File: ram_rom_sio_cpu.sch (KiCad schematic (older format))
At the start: 13 parts, among them U1 SST39SF040, U2 Z84C0010AEG, U3 AS6C4008A-55ZIN, U4 Z84C4310AEG

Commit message: rotated layout
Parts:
- removed JP2: WR Ena, Connector_PinHeader_2.54mm:PinHeader_1x03_P2.54mm_Vertical, symbol Jumper:Jumper_3_Bridged12
- added J4: Port A, Connector_PinHeader_2.54mm:PinHeader_1x06_P2.54mm_Vertical, symbol Connector_Generic:Conn_01x06
- added R10, R7, R8, R9: 10K, Resistor_SMD:R_0603_1608Metric_Pad1.05x0.95mm_HandSolder, symbol Device:R_Small
- added R4, R6: 100K, Resistor_SMD:R_0603_1608Metric_Pad1.05x0.95mm_HandSolder, symbol Device:R_Small
- RN2: value 10K -> 2K2
- renumbered C3 to C2, C4 to C3, C5 to C4, C6 to C5, R9 to R2, R10 to R3, R11 to R5
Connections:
- net labels added: RX, TX, ~CTS, ~RTS
- net labels removed: RXA, ~CTSA, ~RTSA
- wire segments 157 -> 180
- no-connect marks 15 -> 16

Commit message: Routing completed, fixed RAM/ROM paging
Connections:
- net labels added: A[0..15], MA14, MA15, MA16, MA17, MA18, MA[14..18]
- net labels removed: A16, A17, A18, A[0..18], TXA
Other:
- moved on the sheet: R2

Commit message: added gnd plane stitching
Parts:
- U1: footprint Package_LCC:PLCC-32_11.4x14.0mm_P1.27mm -> Package_LCC:PLCC-32_11.4x14.0mm_P1.27mm-Socket
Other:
- note added: "SRAM 512K"
- moved on the sheet: C2, C3, C4, C5, J4, R2, R3, R4, R5, R6, RN2, U3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

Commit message: enhanced graphic for PLCC socket
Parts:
- removed U1: SST39SF040, Package_LCC:PLCC-32_11.4x14.0mm_P1.27mm-Socket, symbol Memory_Flash:SST39SF040
- added U?: SST39LF040, Package_LCC:PLCC-32_11.4x14.0mm_P1.27mm-Socket, symbol Memory_Flash:SST39LF040
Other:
- moved on the sheet: R2
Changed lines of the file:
@@
 L Device:R_Small R2
 U 1 1 5D959555
-P 10300 2000
-F 0 "R2" H 10359 2046 50  0000 L CNN
-F 1 "10K" H 10359 1955 50  0000 L CNN
-F 2 "Resistor_SMD:R_0603_1608Metric_Pad1.05x0.95mm_HandSolder" H 10300 2000 50  0001 C CNN
-F 3 "~" H 10300 2000 50  0001 C CNN
-	1    10300 2000
-	-1   0    0    -1
+P 7100 3200
+F 0 "R2" H 7159 3246 50  0000 L CNN
+F 1 "10K" H 7159 3155 50  0000 L CNN
+F 2 "Resistor_SMD:R_0603_1608Metric_Pad1.05x0.95mm_HandSolder" H 7100 3200 50  0001 C CNN
+F 3 "~" H 7100 3200 50  0001 C CNN
+	1    7100 3200
+	1    0    0    -1
 $EndComp
 $Comp
@@
 Text HLabel 9950 1500 2    50   3State ~ 0
 D[0..7]
-Text Label 9500 2100 0    50   ~ 0
+Text Label 7900 3300 2    50   ~ 0
 ROM_~CE
-Text HLabel 9700 2200 2    50   Input ~ 0
+Text HLabel 7700 3400 0    50   Input ~ 0
 ~RD
 Entry Wire Line
@@
 Wire Wire Line
 	9300 1100 9850 1100
-Text HLabel 10400 2100 2    50   Input ~ 0
+Text HLabel 7000 3300 0    50   Input ~ 0
 ROM_~CE~
 Text Notes 8950 900  0    50   ~ 0
 Flash/ROM
-$Comp
-L Memory_Flash:SST39SF040 U1
-U 1 1 5D653323
-P 8700 1950
-F 0 "U1" H 8350 3000 50  0000 C CNN
-F 1 "SST39SF040" H 8750 2000 50  0000 C CNN
-F 2 "Package_LCC:PLCC-32_11.4x14.0mm_P1.27mm-Socket" H 8700 2250 50  0001 C CNN
-F 3 "http://ww1.microchip.com/downloads/en/DeviceDoc/25022B.pdf" H 8700 2250 50  0001 C CNN
-	1    8700 1950
-	1    0    0    -1
-$EndComp
-Wire Wire Line
-	9300 2200 9700 2200
+Wire Wire Line
+	8100 3400 7700 3400
 Wire Wire Line
 	10200 5250 10300 5250
@@
 F 3 "" H 2900 750 50  0001 C CNN
 	1    2900 750
-	1    0    0    -1
-$EndComp
-$Comp
-L power:VCC #PWR?
-U 1 1 5DCF306D
-P 8700 1000
-AR Path="/5DCF306D" Ref="#PWR?"  Part="1"
-AR Path="/5D6224DC/5DCF306D" Ref="#PWR?"  Part="1"
-AR Path="/5F2A9FE8/5DCF306D" Ref="#PWR010"  Part="1"
-F 0 "#PWR010" H 8700 850 50  0001 C CNN
-F 1 "VCC" H 8717 1173 50  0000 C CNN
-F 2 "" H 8700 1000 50  0001 C CNN
-F 3 "" H 8700 1000 50  0001 C CNN
-	1    8700 1000
 	1    0    0    -1
 $EndComp
@@
 Text Label 3850 5550 0    50   ~ 0
 ~CTS
-Text HLabel 9700 2300 2    50   Input ~ 0
+Text HLabel 7700 3100 0    50   Input ~ 0
 ~WR
 Wire Wire Line
-	9300 2300 9700 2300
+	8100 3100 7700 3100
 $Comp
 L Device:R_Small R?
@@
 Text HLabel 7550 5950 0    50   Input ~ 0
 MA[14..18]
-$Comp
-L power:GND #PWR?
-U 1 1 5EB5C154
-P 8700 3050
-AR Path="/5EB5C154" Ref="#PWR?"  Part="1"
-AR Path="/5CB63856/5EB5C154" Ref="#PWR?"  Part="1"
-AR Path="/5CB5AB00/5CB63856/5EB5C154" Ref="#PWR?"  Part="1"
-AR Path="/5CFABACD/5EB5C154" Ref="#PWR?"  Part="1"
-AR Path="/5CF9C1ED/5EB5C154" Ref="#PWR?"  Part="1"
-AR Path="/5D6224DC/5EB5C154" Ref="#PWR?"  Part="1"
-AR Path="/5F2A9FE8/5EB5C154" Ref="#PWR0102"  Part="1"
-F 0 "#PWR0102" H 8700 2800 50  0001 C CNN
-F 1 "GND" H 8705 2877 50  0000 C CNN
-F 2 "" H 8700 3050 50  0001 C CNN
-F 3 "" H 8700 3050 50  0001 C CNN
-	1    8700 3050
-	1    0    0    -1
-$EndComp
-Wire Wire Line
-	9300 2100 10300 2100
-Wire Wire Line
-	10400 2100 10300 2100
-Connection ~ 10300 2100
+Wire Wire Line
+	8100 3300 7100 3300
+Wire Wire Line
+	7000 3300 7100 3300
+Connection ~ 7100 3300
 Text HLabel 7450 2800 0    50   Input ~ 0
 MA[14..18]
@@
 Text Notes 9050 3950 0    50   ~ 0
 SRAM 512K
+$Comp
+L Memory_Flash:SST39LF040 U?
+U 1 1 5EA5881D
+P 8700 2300
+F 0 "U?" H 8700 3781 50  0000 C CNN
+F 1 "SST39LF040" H 8700 3690 50  0000 C CNN
+F 2 "Package_LCC:PLCC-32_11.4x14.0mm_P1.27mm-Socket" H 8700 2600 50  0001 C CNN
+F 3 "http://ww1.microchip.com/downloads/en/DeviceDoc/25022B.pdf" H 8700 2600 50  0001 C CNN
+	1    8700 2300
+	1    0    0    -1
+$EndComp
 Wire Bus Line
 	1550 5700 1550 5850

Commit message: removed ram/rom ce pullups
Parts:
- removed R2, R3: 10K, Resistor_SMD:R_0603_1608Metric_Pad1.05x0.95mm_HandSolder, symbol Device:R_Small
- gave numbers to parts that had none: 1
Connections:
- net labels removed: RAM_~CE, ROM_~CE
- wire segments 180 -> 178
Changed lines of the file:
@@
 Wire Wire Line
 	9200 5350 9750 5350
-Text HLabel 10300 5250 2    50   Input ~ 0
+Text HLabel 9750 5250 2    50   Input ~ 0
 RAM_~CE~
 Text HLabel 9750 5350 2    50   Input ~ 0
@@
 	1    0    0    -1
 $EndComp
-$Comp
-L Device:R_Small R2
-U 1 1 5D959555
-P 7100 3200
-F 0 "R2" H 7159 3246 50  0000 L CNN
-F 1 "10K" H 7159 3155 50  0000 L CNN
-F 2 "Resistor_SMD:R_0603_1608Metric_Pad1.05x0.95mm_HandSolder" H 7100 3200 50  0001 C CNN
-F 3 "~" H 7100 3200 50  0001 C CNN
-	1    7100 3200
-	1    0    0    -1
-$EndComp
-$Comp
-L Device:R_Small R3
-U 1 1 5D966170
-P 10200 5150
-F 0 "R3" H 10259 5196 50  0000 L CNN
-F 1 "10K" H 10259 5105 50  0000 L CNN
-F 2 "Resistor_SMD:R_0603_1608Metric_Pad1.05x0.95mm_HandSolder" H 10200 5150 50  0001 C CNN
-F 3 "~" H 10200 5150 50  0001 C CNN
-	1    10200 5150
-	-1   0    0    -1
-$EndComp
-Text Label 9650 5250 2    50   ~ 0
-RAM_~CE
 Text HLabel 9950 1500 2    50   3State ~ 0
 D[0..7]
-Text Label 7900 3300 2    50   ~ 0
-ROM_~CE
 Text HLabel 7700 3400 0    50   Input ~ 0
 ~RD
@@
 Wire Wire Line
 	9300 1100 9850 1100
-Text HLabel 7000 3300 0    50   Input ~ 0
+Text HLabel 7700 3300 0    50   Input ~ 0
 ROM_~CE~
 Text Notes 8950 900  0    50   ~ 0
@@
 Wire Wire Line
 	8100 3400 7700 3400
-Wire Wire Line
-	10200 5250 10300 5250
 $Comp
 L Device:C_Small C2
@@
 F 3 "" H 8700 4050 50  0001 C CNN
 	1    8700 4050
-	1    0    0    -1
-$EndComp
-$Comp
-L power:VCC #PWR?
-U 1 1 5DCDDE0E
-P 10200 5050
-AR Path="/5DCDDE0E" Ref="#PWR?"  Part="1"
-AR Path="/5D6224DC/5DCDDE0E" Ref="#PWR?"  Part="1"
-AR Path="/5F2A9FE8/5DCDDE0E" Ref="#PWR019"  Part="1"
-F 0 "#PWR019" H 10200 4900 50  0001 C CNN
-F 1 "VCC" H 10217 5223 50  0000 C CNN
-F 2 "" H 10200 5050 50  0001 C CNN
-F 3 "" H 10200 5050 50  0001 C CNN
-	1    10200 5050
 	1    0    0    -1
 $EndComp
@@
 Text HLabel 7550 5950 0    50   Input ~ 0
 MA[14..18]
-Wire Wire Line
-	8100 3300 7100 3300
-Wire Wire Line
-	7000 3300 7100 3300
-Connection ~ 7100 3300
 Text HLabel 7450 2800 0    50   Input ~ 0
 MA[14..18]
-Wire Wire Line
-	9200 5250 10200 5250
-Connection ~ 10200 5250
 Text Notes 9050 3950 0    50   ~ 0
 SRAM 512K
 $Comp
-L Memory_Flash:SST39LF040 U?
+L Memory_Flash:SST39LF040 U1
 U 1 1 5EA5881D
 P 8700 2300
-F 0 "U?" H 8700 3781 50  0000 C CNN
+F 0 "U1" H 8700 3781 50  0000 C CNN
 F 1 "SST39LF040" H 8700 3690 50  0000 C CNN
 F 2 "Package_LCC:PLCC-32_11.4x14.0mm_P1.27mm-Socket" H 8700 2600 50  0001 C CNN
@@
 	1    0    0    -1
 $EndComp
+Wire Wire Line
+	7700 3300 8100 3300
+Wire Wire Line
+	9200 5250 9750 5250
 Wire Bus Line
 	1550 5700 1550 5850

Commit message: added FPGA pin labels
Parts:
- U1: symbol Memory_Flash:SST39LF040 -> SMC-80_DE10-rescue:SST39LF040-Memory_Flash
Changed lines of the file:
@@
 AR Path="/5DFE5C15/5ED989DA" Ref="R?"  Part="1"
 AR Path="/5F2A9FE8/5ED989DA" Ref="R10"  Part="1"
-F 0 "R10" H 5350 2150 50  0000 L CNN
+F 0 "R10" H 5300 2150 50  0000 L CNN
 F 1 "10K" V 5450 2000 30  0000 L CNN
 F 2 "Resistor_SMD:R_0603_1608Metric_Pad1.05x0.95mm_HandSolder" H 5450 2050 50  0001 C CNN
@@
 SRAM 512K
 $Comp
-L Memory_Flash:SST39LF040 U1
+L SMC-80_DE10-rescue:SST39LF040-Memory_Flash U1
 U 1 1 5EA5881D
 P 8700 2300
+AR Path="/5EA5881D" Ref="U1"  Part="1"
+AR Path="/5F2A9FE8/5EA5881D" Ref="U1"  Part="1"
 F 0 "U1" H 8700 3781 50  0000 C CNN
 F 1 "SST39LF040" H 8700 3690 50  0000 C CNN

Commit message: shifted Arduino pins
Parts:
- RN2: Description (none) -> Resistor Networks & Arrays 2.2K OHMS 5% CONV 4RES Anti-Sulf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; Manufacturer_Name (none) -> Bourns; Manufacturer_Part_Number (none) -> CAY16-222J4AS
- U1: Description (none) -> NOR Flash 3.0 to 3.6V 4Mbit Multi-Purpose Flash; Manufacturer_Name (none) -> Microchip; Manufacturer_Part_Number (none) -> SST39LF040-55-4C-NHE
- U3: Description (none) -> SRAM 4M, 2.7-5.5V, 55ns 512K x 8 Asynch SRAM; Manufacturer_Name (none) -> Alliance Memory; Manufacturer_Part_Number (none) -> AS6C4008A-55ZIN
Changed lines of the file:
@@
 F 2 "Package_SO:TSOP-II-32_21.0x10.2mm_P1.27mm" H 8700 5250 50  0001 C CNN
 F 3 "https://www.alliancememory.com/wp-content/uploads/pdf/AS6C4008.pdf" H 8700 5250 50  0001 C CNN
+F 4 "SRAM 4M, 2.7-5.5V, 55ns 512K x 8 Asynch SRAM" H 8700 5150 50  0001 C CNN "Description"
+F 5 "Alliance Memory" H 8700 5150 50  0001 C CNN "Manufacturer_Name"
+F 6 "AS6C4008A-55ZIN" H 8700 5150 50  0001 C CNN "Manufacturer_Part_Number"
 	1    8700 5150
 	1    0    0    -1
@@
 F 1 "2K2" V 4350 6600 50  0000 C CNN
 F 2 "Resistor_SMD:R_Cat16-4" V 5225 6600 50  0001 C CNN
-F 3 "~" H 4750 6600 50  0001 C CNN
+F 3 "https://www.mouser.com/datasheet/2/54/CATCAY-777361.pdf" H 4750 6600 50  0001 C CNN
+F 4 "Resistor Networks & Arrays 2.2K OHMS 5% CONV 4RES Anti-Sulfur" H 4750 6600 50  0001 C CNN "Description"
+F 5 "Bourns" H 4750 6600 50  0001 C CNN "Manufacturer_Name"
+F 6 "CAY16-222J4AS" H 4750 6600 50  0001 C CNN "Manufacturer_Part_Number"
 	1    4750 6600
 	0    1    1    0
@@
 F 2 "Package_LCC:PLCC-32_11.4x14.0mm_P1.27mm-Socket" H 8700 2600 50  0001 C CNN
 F 3 "http://ww1.microchip.com/downloads/en/DeviceDoc/25022B.pdf" H 8700 2600 50  0001 C CNN
+F 4 "NOR Flash 3.0 to 3.6V 4Mbit Multi-Purpose Flash" H 8700 2300 50  0001 C CNN "Description"
+F 5 "Microchip" H 8700 2300 50  0001 C CNN "Manufacturer_Name"
+F 6 "SST39LF040-55-4C-NHE" H 8700 2300 50  0001 C CNN "Manufacturer_Part_Number"
 	1    8700 2300
 	1    0    0    -1

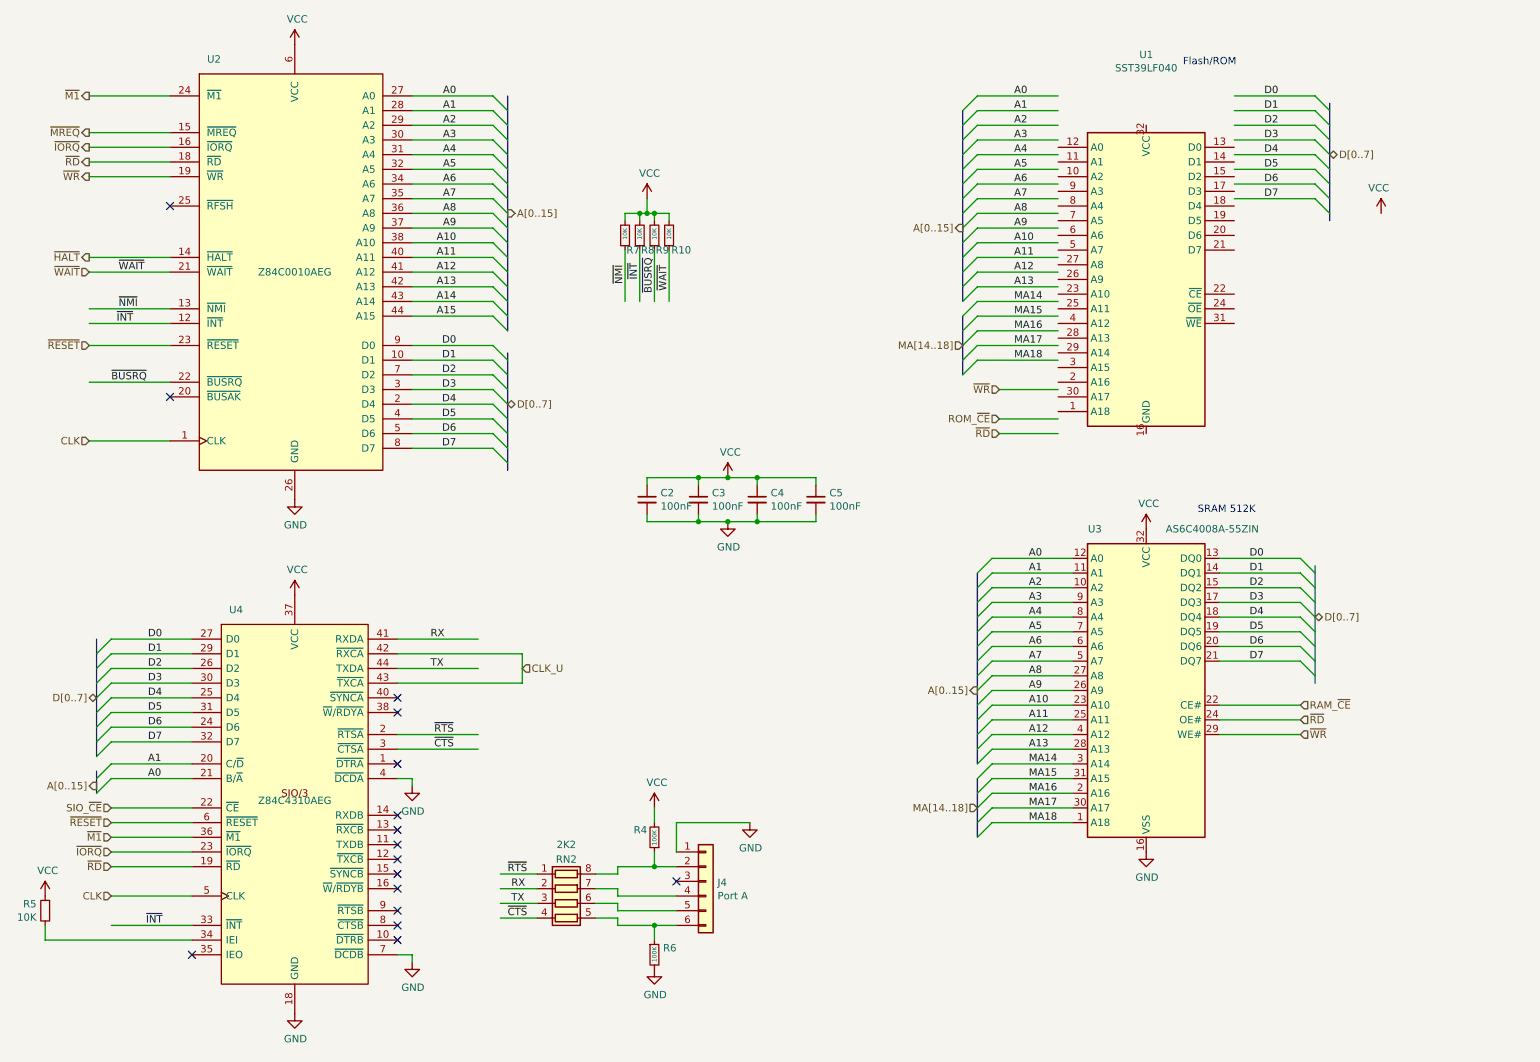
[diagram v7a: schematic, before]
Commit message: normalize symbols
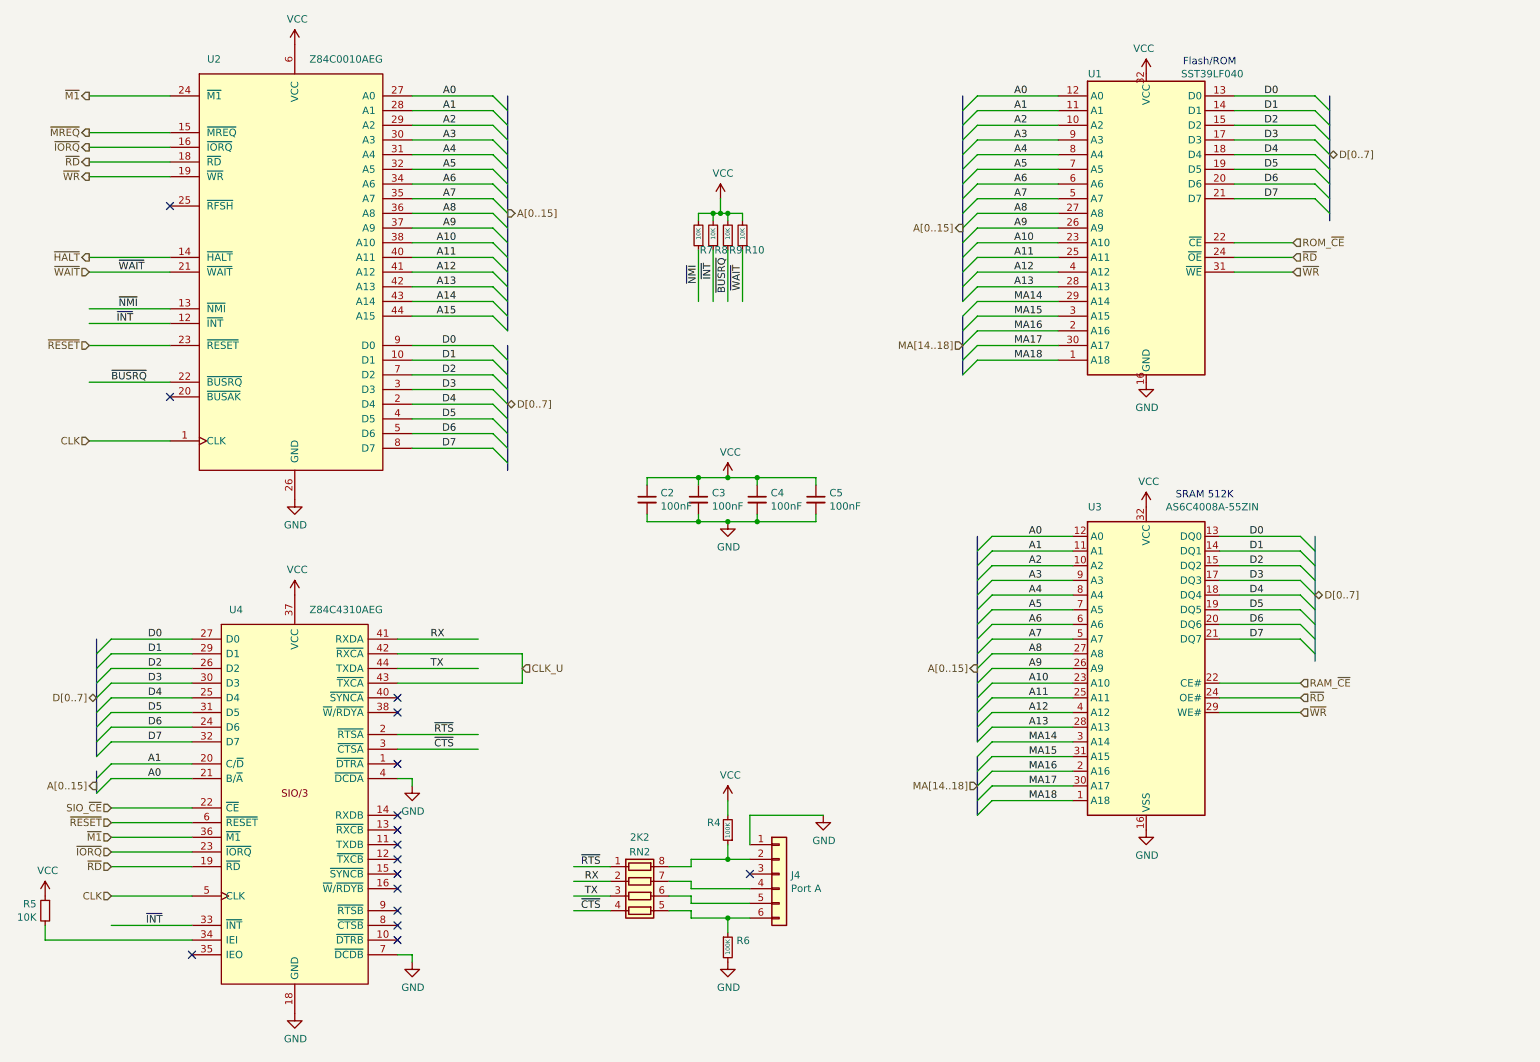
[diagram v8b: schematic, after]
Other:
- moved on the sheet: J4, R10, R4, R6, R7, R8, R9, RN2, U1, U3
